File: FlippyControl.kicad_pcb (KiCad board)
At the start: 2 copper layers, 68.5 x 53.3 mm, 23 parts, among them J1 WiiNunchuck, J2 WiiNunchuck, J3 Data Harness Out, J4 USB_C_Receptacle_USB2.0, P1 Power, P2 Analog, P3 Digital, P4 Digital, P5 CONN_01X01, P7 CONN_01X01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

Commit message: Add submodule and migrate project
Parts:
- D1: footprint Diode_SMD:Nexperia_CFP3_SOD-123W -> Diode_SMD:D_SOD-123
- J1, J2: footprint FlippyControl:WiiNunchuck -> Nieto_Connector:WiiNunchuck
- J4: value USB_C_Receptacle_USB2.0 -> USB4085-GF-A
- U1: value mini_esp32 -> ESP32-D1-Mini; footprint FlippyControl:ESP32_mini -> Nieto_Module:ESP32_mini
- moved J1 0.13 mm to (174.3, 85.2)
- turned TP7 to 180 degrees
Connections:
- net /10(**/SS) renamed NUNCHUCK1_DET
- net /7 renamed NUNCHUCK2_SDA
- net /8 renamed NUNCHUCK2_SCL
- net /9(**) renamed NUNCHUCK2_DET
- net PIN_I2C_SCL renamed NUNCHUCK1_SCL
- net PIN_I2C_SDA renamed NUNCHUCK1_SDA
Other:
- board size 68.5 x 53.3 mm -> 68.6 x 53.3 mm
- board text removed: "(Notch)"

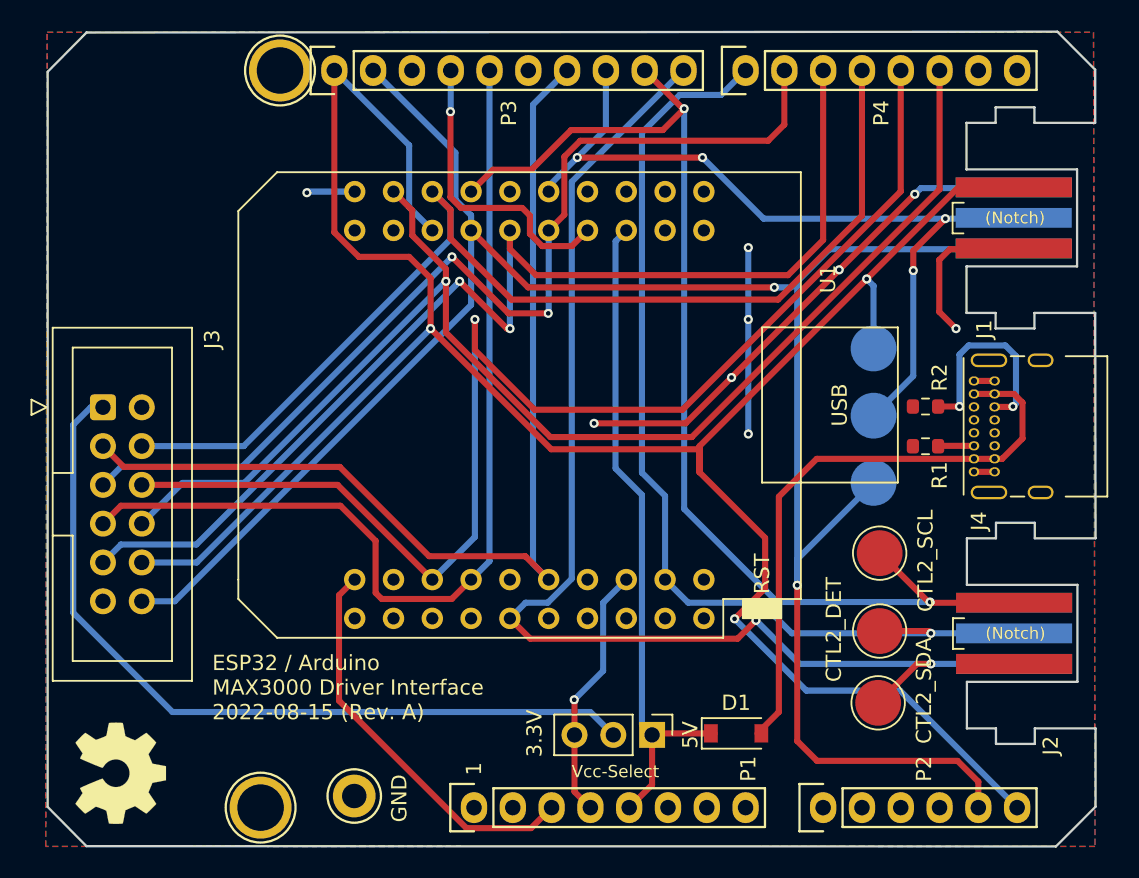
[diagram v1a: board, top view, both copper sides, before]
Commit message: Final Rev.B, adding RasPi connector and PWM output
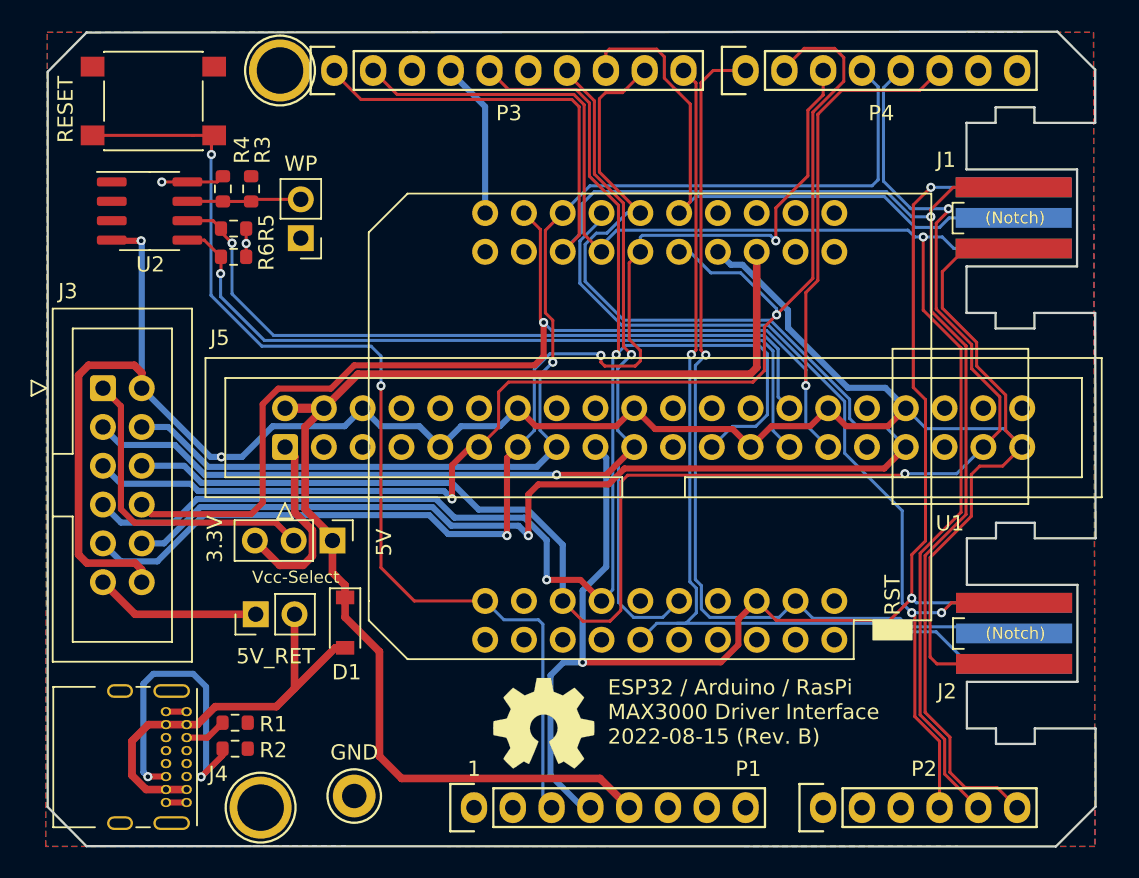
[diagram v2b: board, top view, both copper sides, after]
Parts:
- removed TP1: CTL2_SCL, TestPoint:TestPoint_Pad_D3.0mm
- removed TP2: CTL1_SCL, TestPoint:TestPoint_Pad_D3.0mm
- removed TP3: CTL2_SDA, TestPoint:TestPoint_Pad_D3.0mm
- removed TP4: CTL1_SDA, TestPoint:TestPoint_Pad_D3.0mm
- removed TP5: CTL2_DET, TestPoint:TestPoint_Pad_D3.0mm
- removed TP6: CTL1_DET, TestPoint:TestPoint_Pad_D3.0mm
- added J5: RasPI-40Pin, Connector_IDC:IDC-Header_2x20_P2.54mm_Vertical, F.Cu at (126.6, 100.2)
- added J6: WP, Connector_PinHeader_2.54mm:PinHeader_1x02_P2.54mm_Vertical, F.Cu at (127.6, 86.5)
- added JP2: 5V_RET, Connector_PinHeader_2.54mm:PinHeader_1x02_P2.54mm_Vertical, F.Cu at (124.6, 111.2)
- added R3: DNP, Resistor_SMD:R_0603_1608Metric, F.Cu at (124.3, 83.3)
- added R4: 10K, Resistor_SMD:R_0603_1608Metric, F.Cu at (122.5, 83.3)
- added R5: 5.1k, Resistor_SMD:R_0603_1608Metric, F.Cu at (123.2, 85.9)
- added R6: 5.1k, Resistor_SMD:R_0603_1608Metric, F.Cu at (123.2, 87.8)
- added SW1: RESET, Button_Switch_SMD:SW_SPST_PTS645, F.Cu at (117.9, 77.6)
- added U2: CAT24C32, Package_SO:SOIC-8_3.9x4.9mm_P1.27mm, F.Cu at (117.7, 84.8)
- moved J4 53.9 mm to (120.1, 117.5), turned to -90 degrees
- moved R2 50.4 mm to (123.3, 120.0), turned to 0 degrees
- moved R1 48.7 mm to (123.3, 118.3), turned to 0 degrees
- moved REF** 27.9 mm to (143.5, 118.3), turned to 0 degrees
- moved D1 26.6 mm to (130.5, 111.7), turned to -90 degrees
- moved JP1 24.5 mm to (129.7, 106.3)
- moved U1 8.65 mm to (151.1, 98.9)
- moved J3 1.25 mm to (114.6, 96.4)
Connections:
- net COL_PULSE_N renamed MAX3000_COL
- net MTX_CLK renamed MAX3000_SCK
- net MTX_DOUT renamed MAX3000_MOSI
- net MTX_LATCH renamed MAX3000_LATCH
- net MTX_RST renamed MAX3000_RST
- net PULSE_ENABLE_IN renamed MAX3000_PULSE
- net ROW_PULSE_N renamed MAX3000_ROW
- J3 pad 10: NUNCHUCK1_SCL -> MAX3000_LED_PWM
- J3 pad 11: unconnected-(J3-Pad11) -> MAX3000_AUX_5V
- J3 pad 12: NUNCHUCK1_SDA -> GND
- P2 pad 4: /A3 -> NUNCHUCK2_DET
- P3 pad 9: NUNCHUCK2_DET -> MAX3000_LED_PWM
- U1 pad 30: unconnected-(U1-Pad30) -> MAX3000_LED_PWM
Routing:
- net GND: track 48.0 -> 174.3 mm, vias 6 -> 2
- net MAX3000_LED_PWM: track 0.00 -> 101.2 mm, vias 0 -> 1
- net +3V3: track 50.8 -> 111.7 mm
- net EEPROM_SDA: track 0.00 -> 49.6 mm, vias 0 -> 1
- net EEPROM_SCL: track 0.00 -> 48.4 mm, vias 0 -> 1
- net NUNCHUCK1_SDA: track 142.3 -> 94.2 mm, vias 2 -> 1
- net NUNCHUCK1_SCL: track 152.2 -> 105.5 mm, vias 3 -> 1
- net /Reset: track 26.3 -> 69.5 mm, vias 0 -> 2
- net +5V: track 43.8 -> 82.6 mm
- net MAX3000_SCK: track 63.5 -> 98.2 mm, vias 0 -> 2
- net Net-(J3-Pad1): track 53.4 -> 20.6 mm
- net MAX3000_LATCH: track 66.4 -> 86.1 mm
- net NUNCHUCK2_SCL: track 81.2 -> 63.7 mm, vias 2 -> 1
- net MAX3000_COL: track 85.1 -> 101.9 mm, vias 1 -> 2
- net NUNCHUCK1_DET: track 54.7 -> 40.0 mm, vias 4 -> 0
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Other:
- rule pad_to_mask_clearance: 0.05 -> 0
- board text added: "ESP32 / Arduino / RasPi MAX3000 Driver Interface 2022-08-15 (Rev. B)"
- board text removed: "ESP32 / Arduino MAX3000 Driver Interface 2022-08-15 (Rev. A)"

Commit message: Add pullups, fix miswired pads
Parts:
- added R10: 4.7k, Resistor_SMD:R_0603_1608Metric, F.Cu at (154.9, 79.4)
- added R11: 4.7k, Resistor_SMD:R_0603_1608Metric, F.Cu at (156.7, 79.3)
- added R12: 4.7k, Resistor_SMD:R_0603_1608Metric, F.Cu at (167.5, 120.9)
- added R7: 4.7k, Resistor_SMD:R_0603_1608Metric, F.Cu at (144.4, 79.3)
- added R8: 4.7k, Resistor_SMD:R_0603_1608Metric, F.Cu at (142.7, 79.3)
- added R9: 4.7k, Resistor_SMD:R_0603_1608Metric, F.Cu at (148.2, 79.4)
- R5, R6: value 5.1k -> 3.9k
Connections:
- J2 pad 2: NUNCHUCK2_SDA -> NUNCHUCK2_DET
- J2 pad 3: NUNCHUCK2_DET -> NUNCHUCK2_SCL
- J2 pad 5: NUNCHUCK2_SCL -> NUNCHUCK2_SDA
- J5 pad 12: unconnected-(J5-Pad12) -> MAX3000_LED_PWM
- J5 pad 33: MAX3000_LED_PWM -> unconnected-(J5-Pad33)
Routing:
- net MAX3000_LED_PWM: track 101.2 -> 74.0 mm, vias 1 -> 4
- net +3V3: track 111.7 -> 120.7 mm, vias 5 -> 11
- net NUNCHUCK2_SDA: track 60.3 -> 65.3 mm
- net NUNCHUCK2_SCL: track 63.7 -> 68.4 mm, vias 1 -> 3
- net NUNCHUCK1_SDA: track 94.2 -> 98.1 mm, vias 1 -> 3
- net NUNCHUCK2_DET: track 61.9 -> 65.4 mm, vias 2 -> 1
- net NUNCHUCK1_DET: track 40.0 -> 43.2 mm, vias 0 -> 1
- net NUNCHUCK1_SCL: track 105.5 -> 106.8 mm
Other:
- board text added: "ESP32 / Arduino / RasPi MAX3000 Driver Interface 2023-03-06 (Rev. C)"
- board text removed: "ESP32 / Arduino / RasPi MAX3000 Driver Interface 2022-08-15 (Rev. B)"
